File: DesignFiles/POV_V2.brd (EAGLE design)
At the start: 99.2 x 49.6 mm, 42 parts, among them CN1 1X4-CLEANBIG, CN2 1X4-CLEANBIG, CN3 1X4-CLEANBIG, CN4 1X4-CLEANBIG, IC1 SN74HC595, J1 PINHD-1X10, J2 PINHD-1X10

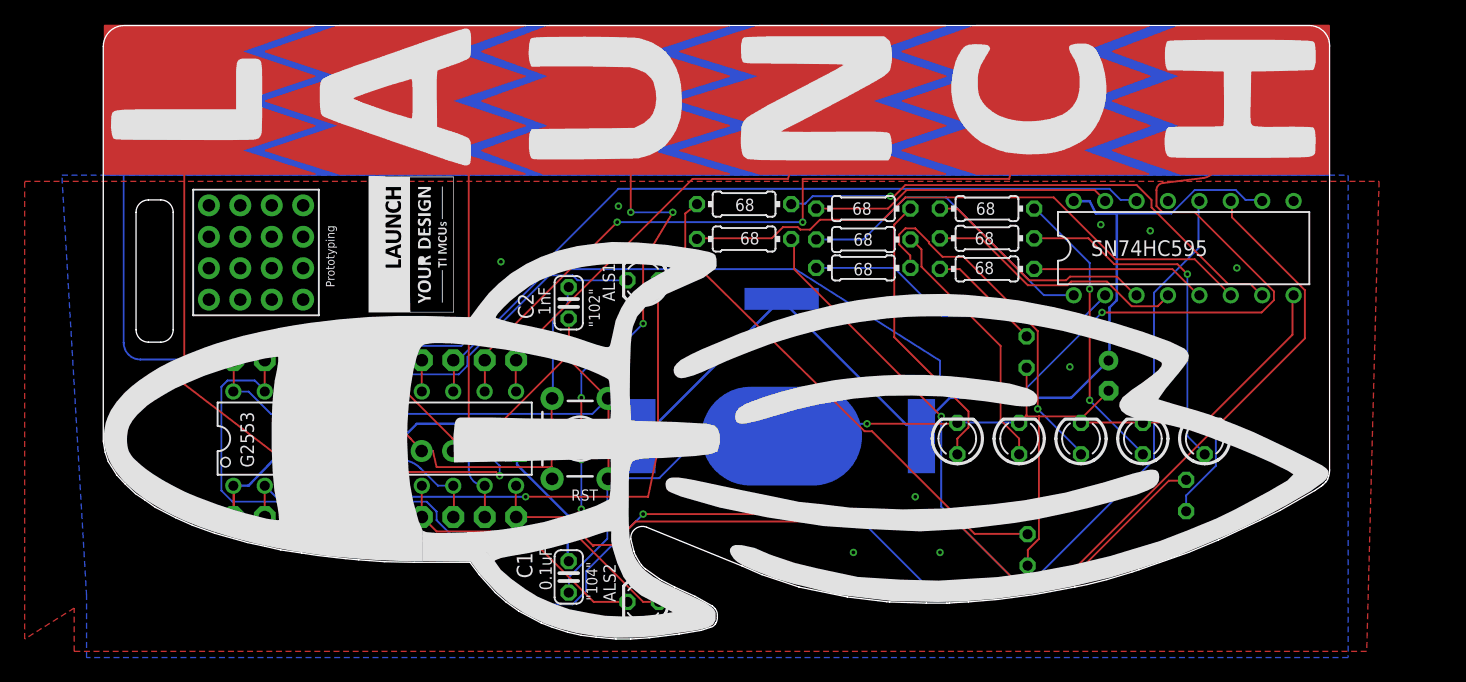
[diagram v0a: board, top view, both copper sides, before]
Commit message: Had incorrect version of board uploaded
Correcting uploaded eagle board
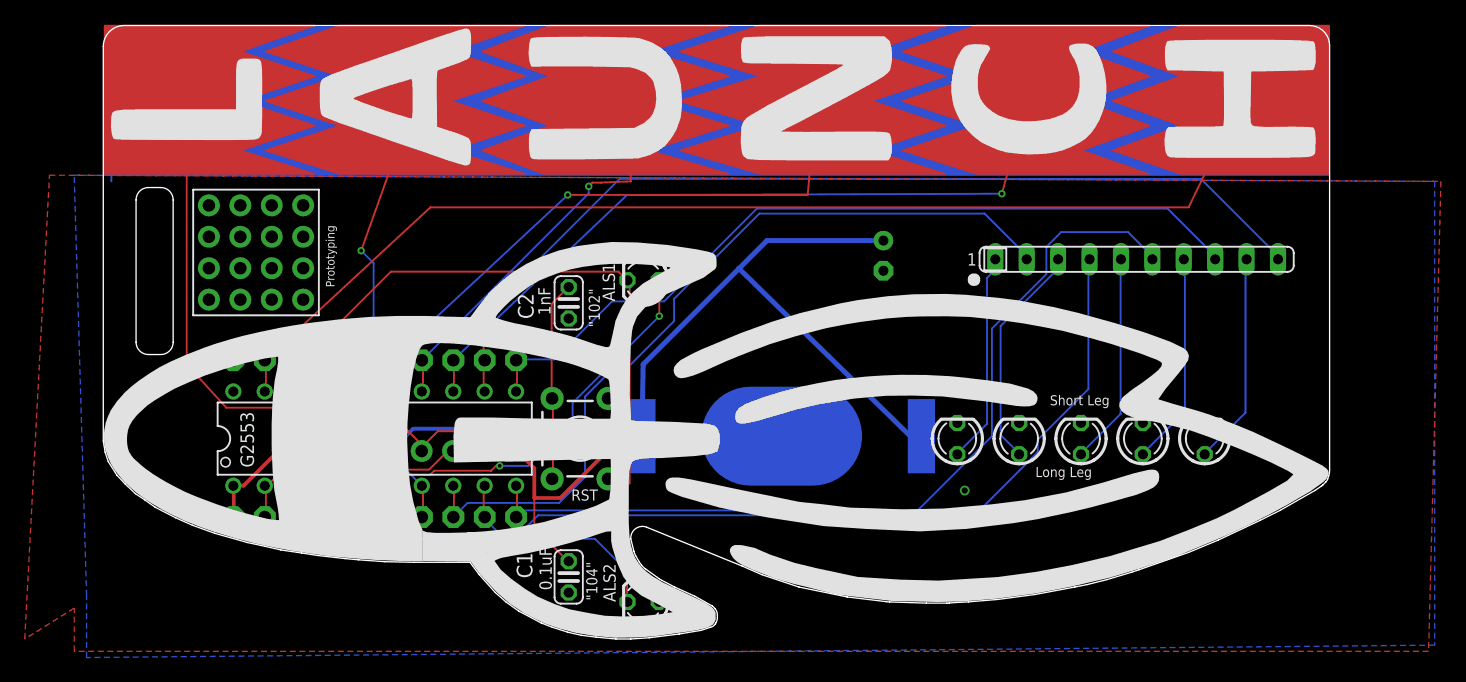
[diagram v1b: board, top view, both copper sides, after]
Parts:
- removed IC1: SN74HC595, TIBadgeCustom:DIL16
- removed LED6, LED7, LED8: (no value), led:LED3MM
- removed R2, R3, R4, R5, R6, R7, R8, R9: 68ohm, resistor:0204/7
- removed U$10: (no value), sti_logo:LOGO16_TPLACE
- removed U$9: (no value), TIBadgeCustom:LYD_FULL
- added RN1: (no value), resistor-sil:SIL10
- PROGRAMMING_HEADER: device BergCustom:1X04-CLEANBIG -> TIBadgeCustom:1X04-CLEANBIG
- R1: device rcl:0204/7 -> TIBadgeCustom:0204/7
- U$3: device ohw-logo:OSHW_FILLX150_NOTEXT -> TIBadgeCustom:BADGE_BACK_REVERSE
- U$6: device TIBadgeCustom:LAUNCH_CIRCUIT_OVERLAY -> TIBadgeCustom:LAUNCH_CIRCUIT_OVERLAY2
- U$7: device BergLogos:BERG_TI_SILK -> 43oh_logo:CIRCUIT_LOG_STOP_ONLY
- U$8: device 43oh_logo:43OH_CIRCUIT_LOGO_LONG -> 43oh_logo:CIRCUIT_LOG_STOP_ONLY
- moved U$3 48.7 mm to (0.13, 0.25), flipped to the top, turned to 0 degrees
- moved U$7 42.3 mm to (5.94, 17.0)
- moved U$8 40.2 mm to (67.5, 6.81), turned to 180 degrees
- moved C3 20.6 mm to (63.4, 31.5)
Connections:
- removed net N$10: IC1.3, R5.2
- removed net N$11: IC1.4, R6.2
- removed net N$13: LED6.A, R7.1
- removed net N$14: LED7.A, R8.1
- removed net N$15: LED8.A, R9.1
- removed net N$16: IC1.5, R7.2
- removed net N$17: IC1.6, R8.2
- removed net N$18: IC1.7, R9.2
- removed net N$6: LED5.A, R6.1
- removed net N$7: IC1.15, R2.2
- removed net N$8: IC1.1, R3.2
- removed net N$9: IC1.2, R4.2
- new net N$1: LED1.A, RN1.1
- net 1.4: now also U$5.L
- net 1.5: now also U$5.A; no longer IC1.11
- net 1.6: now also U$5.U
- net 1.7: now also U$5.N; no longer IC1.14
- net 2.0: now also RN1.2; no longer U$5.L
- net 2.1: now also RN1.4; no longer U$5.A
- net 2.2: now also RN1.6; no longer U$5.U
- net 2.3: now also RN1.8; no longer U$5.N
- net 2.4: now also RN1.10; no longer U$5.C
- net 2.5: now also U$5.C; no longer U$5.H
- net 2.6: now also U$5.H; no longer IC1.12
- net GND: no longer IC1.13, IC1.8, LED6.K, LED7.K, LED8.K
- net N$2: now also LED2.A, RN1.3; no longer LED1.A, R2.1
- net N$3: now also LED3.A, RN1.5; no longer LED2.A, R3.1
- net N$4: now also LED4.A, RN1.7; no longer LED3.A, R4.1
- net N$5: now also LED5.A, RN1.9; no longer LED4.A, R5.1
- net VCC: no longer BAT1.VCC3, IC1.10, IC1.16
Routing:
- net GND: track 201.9 -> 1.04 mm, vias 12 -> 1
- net 1.5: track 99.2 -> 36.5 mm, vias 0 -> 1
- net N$14: track 52.7 -> 0.00 mm, vias 2 -> 0
- net N$17: track 48.0 -> 0.00 mm
- net 2.5: track 107.0 -> 60.2 mm
- net N$18: track 42.8 -> 0.00 mm, vias 1 -> 0
- net 1.4: track 2.55 -> 45.0 mm, vias 0 -> 1
- net N$15: track 41.5 -> 0.00 mm
- net 2.6: track 128.1 -> 91.8 mm, vias 2 -> 0
- net 1.6: track 2.53 -> 34.6 mm, vias 0 -> 1
- net 2.1: track 36.8 -> 68.2 mm, vias 1 -> 0
- net VCC: track 129.7 -> 99.4 mm, vias 0 -> 1
- net N$6: track 28.7 -> 0.00 mm, vias 1 -> 0
- net 2.3: track 37.6 -> 66.1 mm
- net N$9: track 25.7 -> 0.00 mm
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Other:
- board text added: "Long Leg"
- board text added: "Short Leg"
- board text removed: "68"
- board text removed: "Fix TI logo on bottom - needs to be a polygon"
